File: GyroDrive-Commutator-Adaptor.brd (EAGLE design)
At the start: 127 x 76.2 mm, 30 parts, among them IC1 INA2141U, IC2 INA2141U, IC3 INA2141U

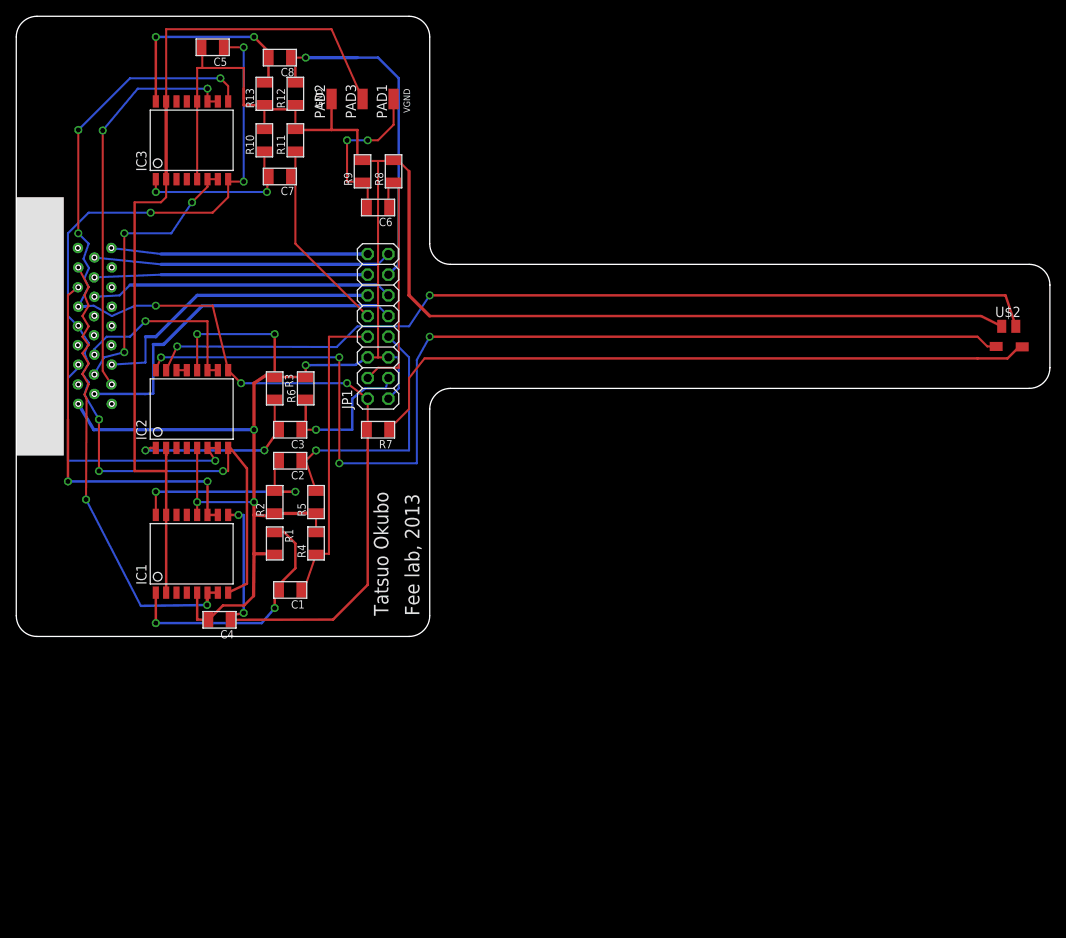
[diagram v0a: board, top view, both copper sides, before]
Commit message: Removed VGROUND and changed JMP1 pinout
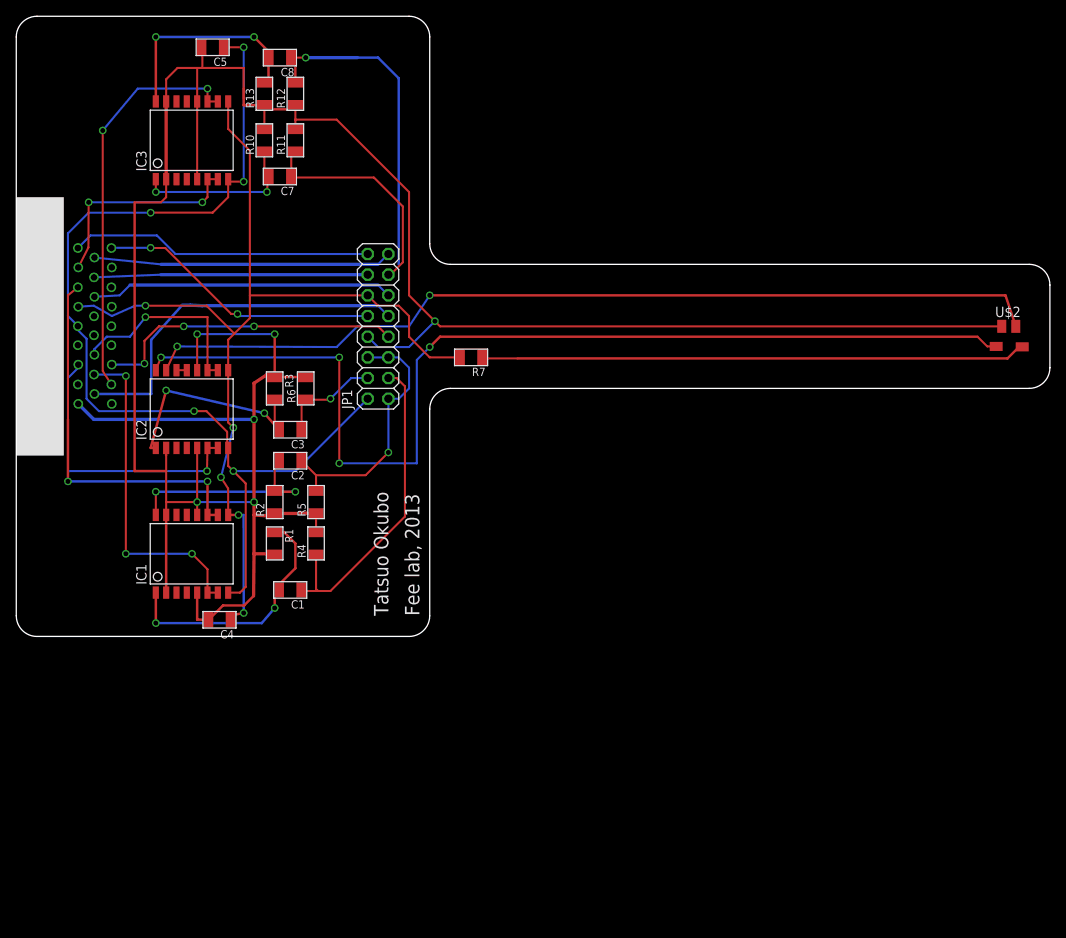
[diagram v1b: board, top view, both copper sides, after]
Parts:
- removed C6: 47nF, elm:R0805ELM
- removed PAD1, PAD2, PAD3: (no value), wirepad:SMD1,27-2,54
- removed R8: 22k, elm:R0805ELM
- removed R9: 1.5M, elm:R0805ELM
- moved R7 14.5 mm to (55.9, 34.3)
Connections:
- net STIM1OUT renamed SCL
- removed net FILTERED_VGROUND: C6.2, PAD1.1, R9.1
- removed net SIGNAL_GROUND: IC1.15, IC1.2, IC2.2, IC3.15, IC3.2, PAD3.1
- removed net STIM1IN: JP1.16, U$3._D
- removed net VGROUND: C6.1, JP1.4, R8.1
- new net DGND: JP1.16, U$3._C
- new net SDA: JP1.10, U$3._D
- net CHAN1: now also IC3.6, IC3.7; no longer IC1.6, IC1.7
- net CHAN4: now also IC1.6, IC1.7; no longer IC3.6, IC3.7
- net E1: now also C7.1, JP1.13, R11.1; no longer C1.1, JP1.8, R4.1
- net E2: now also JP1.1, JP1.5, JP1.6; no longer JP1.7
- net E3: now also JP1.4; no longer JP1.3
- net E4: now also C1.1, JP1.3, R4.1; no longer C7.1, JP1.10, R11.1
- net E5: no longer JP1.13
- net GROUND: now also IC1.15, IC1.2, IC2.2, IC3.15, IC3.2, JP1.8; no longer JP1.1, JP1.5, JP1.6, PAD2.1, R8.2, R9.2
- net ICOM: now also JP1.7; no longer JP1.12
- net V+: now also JP1.12; no longer JP1.2
- net V-: now also JP1.2
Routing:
- net SIGNAL_GROUND: track 110.1 -> 0.00 mm
- net GROUND: track 312.1 -> 352.5 mm
- net DGND: track 0.00 -> 37.2 mm
- net SDA: track 0.00 -> 35.0 mm, vias 0 -> 2
- net VGROUND: track 31.7 -> 0.00 mm
- net STIM1IN: track 31.5 -> 0.00 mm
- net CHAN1: track 56.6 -> 26.6 mm
- net V+: track 148.6 -> 121.2 mm, vias 8 -> 5
- net FILTERED_VGROUND: track 21.1 -> 0.00 mm, vias 2 -> 0
- net V+_HALL: track 84.6 -> 67.0 mm
- net E4: track 24.7 -> 39.5 mm
- net V-: track 116.0 -> 127.7 mm, vias 6 -> 5
- net E1: track 37.7 -> 27.8 mm
- net E3: track 19.6 -> 12.6 mm
- net CHAN4: track 34.9 -> 40.8 mm
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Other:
- board text removed: "GND"
- board text removed: "VGND"

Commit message: Made board into 4 layers. Put in resistors for voltage dividers
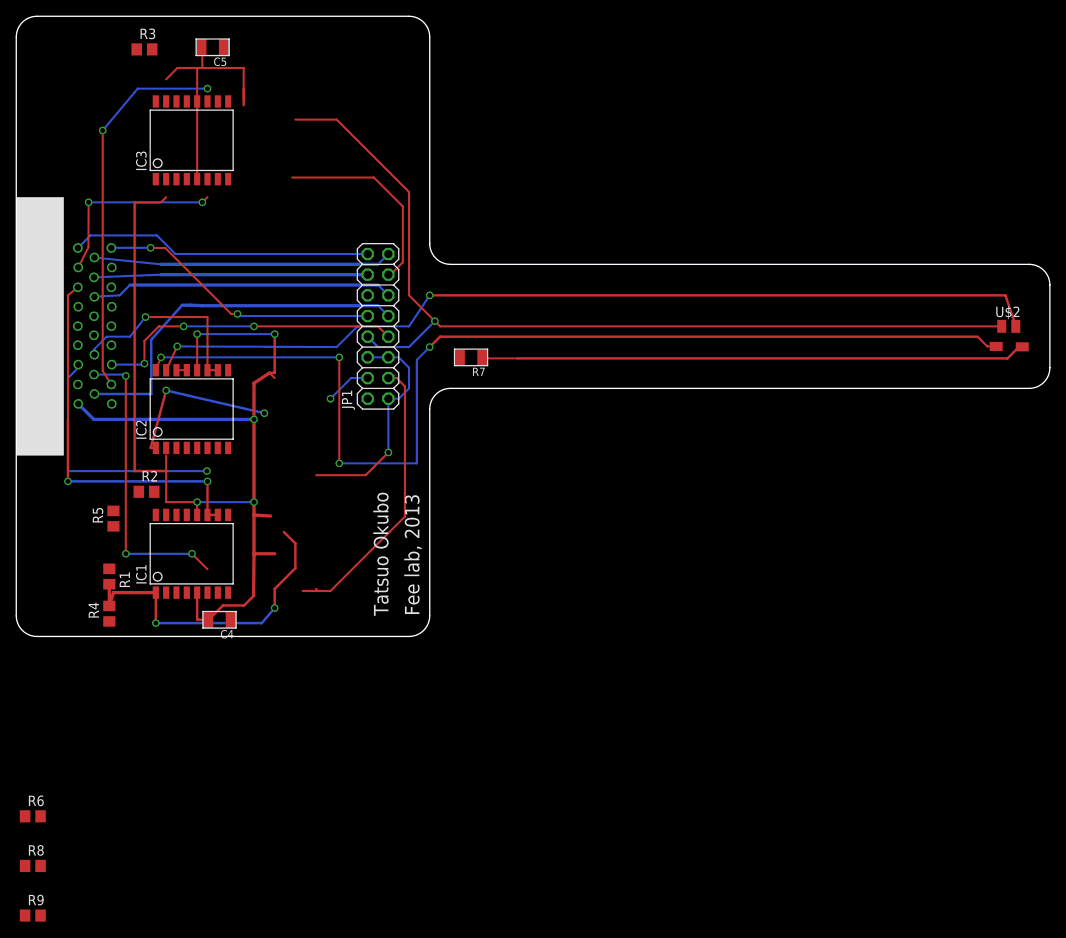
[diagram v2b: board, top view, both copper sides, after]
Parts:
- removed C1, C2, C3, C7, C8: 47nF, elm:R0805ELM
- removed R10, R13: 1.5M, elm:R0805ELM
- removed R11, R12: 22k, elm:R0805ELM
- added R8: 357k, resistor:R0805
- added R9: 3.6k, resistor:R0805
- R1: value 1.5M -> 3.6k; device elm:R0805ELM -> resistor:R0805
- R2, R3: value 1.5M -> 357k; device elm:R0805ELM -> resistor:R0805
- R4: value 22k -> 357k; device elm:R0805ELM -> resistor:R0805
- R5, R6: value 22k -> 3.6k; device elm:R0805ELM -> resistor:R0805
- moved R6 62.4 mm to (2.03, -22.1), turned to 0 degrees
- moved R3 44.6 mm to (15.7, 72.1), turned to 0 degrees
- moved R4 26.8 mm to (11.4, 2.79)
- moved R5 25.0 mm to (11.9, 14.5)
- moved R1 20.7 mm to (11.4, 7.37)
- moved R2 15.8 mm to (16.0, 17.8), turned to 0 degrees
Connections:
- removed net E5: C8.1, R12.2
- removed net GROUND: C4.2, C5.2, IC1.12, IC1.15, IC1.2, IC1.5, IC2.12, IC2.2, IC2.5, IC3.12, IC3.15, IC3.2, IC3.5, JP1.8, R1.2, R10.2, R11.2, R12.1, R13.1, R2.1, R3.1, R4.2, R5.1, R6.2, U$2.A, U$3.A
- removed net N$3: C2.2, IC1.16, R2.2
- removed net N$7: C8.2, IC3.16, R13.2
- removed net N$8: C7.2, IC3.1, R10.1
- new net AGND: C4.2, C5.2, IC1.12, IC1.15, IC1.2, IC1.5, IC2.12, IC3.12, IC3.15, IC3.2, IC3.5, JP1.8, R1.1, R5.1, R6.1, R9.1, U$2.A, U$3.A
- new net V-_INA1: IC1.16, R2.2, R5.2
- new net V-_INA2: IC3.1, R3.2, R6.2
- new net V-_INA3: IC3.16, R8.2, R9.2
- net CHAN1: now also IC1.6, IC1.7; no longer IC3.6, IC3.7
- net CHAN3: now also IC3.6, IC3.7; no longer IC2.6, IC2.7
- net CHAN4: now also IC3.10, IC3.11; no longer IC1.6, IC1.7
- net CHAN5: no longer IC3.10, IC3.11
- net E1: now also R4.1; no longer C7.1, R11.1
- net E2: now also R2.1; no longer C2.1, R5.2
- net E3: now also R3.1; no longer C3.1, R6.1
- net E4: now also R8.1; no longer C1.1, R4.1
- net V-_INA: now also R1.2, R4.2; no longer C1.2, R1.1
- net V-_INC: no longer C3.2, R3.2
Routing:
- net GROUND: track 352.5 -> 0.00 mm, vias 6 -> 0
- net AGND: track 0.00 -> 293.6 mm, vias 0 -> 6
- net V-: track 127.7 -> 0.00 mm, vias 5 -> 0
- net V+: track 121.2 -> 0.00 mm, vias 5 -> 0
- net E5: track 40.2 -> 0.00 mm, vias 1 -> 0
- net N$7: track 26.8 -> 0.00 mm, vias 2 -> 0
- net N$3: track 26.5 -> 0.00 mm, vias 2 -> 0
- net N$8: track 21.6 -> 0.00 mm, vias 2 -> 0
- net V-_INA: track 31.8 -> 39.8 mm
- net V-_INC: track 27.4 -> 20.3 mm
- net E3: track 12.6 -> 5.80 mm
- net E2: track 32.4 -> 27.9 mm
- net E4: track 39.5 -> 35.2 mm
- net CHAN4: track 40.8 -> 36.7 mm
- net CHAN3: track 34.8 -> 30.7 mm
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- added copper zone on layer 15, net AGND

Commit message: Finished routing
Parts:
- removed IC1, IC2, IC3: INA2141U, burr-brown:SO16-1
- removed U$3: MMD1P22G-26-M101, elm:MMD1P22G-26-M101
- added C1, C2, C3, C6: (no value), resistor:C0402
- added U$1: NORCOMP-DB25-SMD-MALE, michael-stetner:190-025-163R001
- added U1, U2, U3: INA2141U, burr-brown:SO16-1
- added U4: PCA9517, PCA9517:SO-08
- added U5: 5V, michael-stetner:SC70
- added U6: 2.5V, michael-stetner:SC70
- moved R9 92.1 mm to (15.1, 56.9), turned to 180 degrees
- moved R8 86.8 mm to (19.1, 56.9), turned to 180 degrees
- moved C5 57.5 mm to (8.26, 17.2), turned to 270 degrees
- moved R6 50.5 mm to (15.1, 26.7), turned to 180 degrees
- moved R3 45.5 mm to (19.1, 26.7), turned to 180 degrees
- moved R4 18.9 mm to (19.1, 20.1), turned to 180 degrees
- moved C4 17.7 mm to (8.24, 7.75), turned to 90 degrees
- moved JP1 17.3 mm to (27.2, 38.1)
- moved R2 13.4 mm to (19.1, 4.80), turned to 180 degrees
- moved R1 13.2 mm to (15.1, 20.1), turned to 0 degrees
- moved R5 10.2 mm to (15.1, 4.80), turned to 180 degrees
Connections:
- removed net CHAN5: U$3.F
- removed net GAIN_HALL: IC2.13, IC2.14
- removed net MOTOR_GROUND: U$3._B
- removed net SCL: JP1.15, U$3._A
- removed net SDA: JP1.10, U$3._D
- removed net STIM2IN: JP1.11, U$3.U
- removed net STIM2OUT: JP1.14, U$3.X
- removed net V-_INA: IC1.1, R1.2, R4.2
- removed net V-_INA1: IC1.16, R2.2, R5.2
- removed net V-_INA2: IC3.1, R3.2, R6.2
- removed net V-_INA3: IC3.16, R8.2, R9.2
- removed net V-_INC: IC2.1
- new net +2.5V: C6.1, U4.1, U6.5
- new net +5V: C1.1, U4.5, U4.8, U5.5
- new net IN1: R2.2, R5.1, U1.15
- new net IN2: R1.2, R4.2, U1.2
- new net IN3: R3.2, R6.1, U2.15
- new net IN4: R8.2, R9.1, U3.2
- new net MOTORGND: U$1.P$18
- new net N$1: U2.6, U2.7
- new net N$3: U3.13, U3.14
- new net SCL_BIRD: JP1.16, U4.2
- new net SCL_RIG: U$1.P$22, U4.7
- new net SDA_BIRD: JP1.15, U4.3
- new net SDA_RIG: U$1.P$21, U4.6
- new net STIMIN: JP1.5, U$1.P$23
- new net STIMOUT: JP1.3, U$1.P$24
- net AGND: now also JP1.10, JP1.11, R5.2, R6.2, R9.2, U$1.P$10, U1.1, U1.12, U1.16, U1.5, U2.1, U2.12, U2.16, U2.2, U3.1, U3.12, U3.5; no longer IC1.12, IC1.15, IC1.2, IC1.5, IC2.12, IC3.12, IC3.15, IC3.2, IC3.5, JP1.8, R5.1, R6.1, R9.1, U$3.A
- net CHAN1: now also U$1.P$13, U1.10, U1.11; no longer IC1.6, IC1.7, U$3.Z
- net CHAN2: now also U$1.P$12, U1.6, U1.7; no longer IC1.10, IC1.11, U$3.W
- net CHAN3: now also U$1.P$11, U2.10, U2.11; no longer IC3.6, IC3.7, U$3.H
- net CHAN4: now also U$1.P$16, U3.6, U3.7; no longer IC3.10, IC3.11, U$3.E
- net DGND: now also C1.2, C2.2, C3.2, C6.2, JP1.13, JP1.14, U$1.P$15, U4.4, U5.2, U6.2; no longer JP1.16, U$3._C
- net E1: now also JP1.1, R2.1; no longer JP1.13, R4.1
- net E2: now also JP1.2, R4.1; no longer JP1.1, JP1.5, JP1.6, R2.1
- net E4: now also JP1.12; no longer JP1.3
- net HALL: now also U$1.P$4, U3.10, U3.11; no longer IC2.10, IC2.11, U$3.J
- net HALL0: now also U3.16; no longer IC2.16
- net HALL1: now also U3.15; no longer IC2.15
- net ICOM: now also JP1.6, U$1.P$5; no longer JP1.7, U$3.K
- net IX: now also JP1.8, U$1.P$17; no longer JP1.9, U$3.B
- net V+: now also C2.1, C3.1, JP1.9, U$1.P$1, U1.9, U2.9, U3.9, U5.4, U6.4; no longer IC1.9, IC2.9, IC3.9, JP1.12, U$3.T
- net V-: now also JP1.7, U$1.P$2, U1.8, U2.8, U3.8; no longer IC1.8, IC2.8, IC3.8, JP1.2, U$3.P
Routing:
- net V+: track 0.00 -> 185.1 mm, vias 0 -> 5
- net AGND: track 293.6 -> 116.9 mm, vias 6 -> 14
- net V-: track 0.00 -> 73.9 mm, vias 0 -> 5
- net SCL_RIG: track 0.00 -> 53.5 mm, vias 0 -> 2
- net SDA_RIG: track 0.00 -> 50.1 mm, vias 0 -> 2
- net CHAN5: track 46.8 -> 0.00 mm, vias 2 -> 0
- net V-_INA: track 39.8 -> 0.00 mm, vias 2 -> 0
- net STIM2IN: track 37.2 -> 0.00 mm
- net SCL: track 36.7 -> 0.00 mm
- net SDA: track 35.0 -> 0.00 mm, vias 2 -> 0
- net STIM2OUT: track 33.6 -> 0.00 mm
- net STIMOUT: track 0.00 -> 33.0 mm, vias 0 -> 1
- net SDA_BIRD: track 0.00 -> 29.1 mm, vias 0 -> 1
- net STIMIN: track 0.00 -> 28.7 mm, vias 0 -> 1
- net CHAN2: track 47.0 -> 19.2 mm, vias 2 -> 0
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- added copper zone on layer 15, net DGND

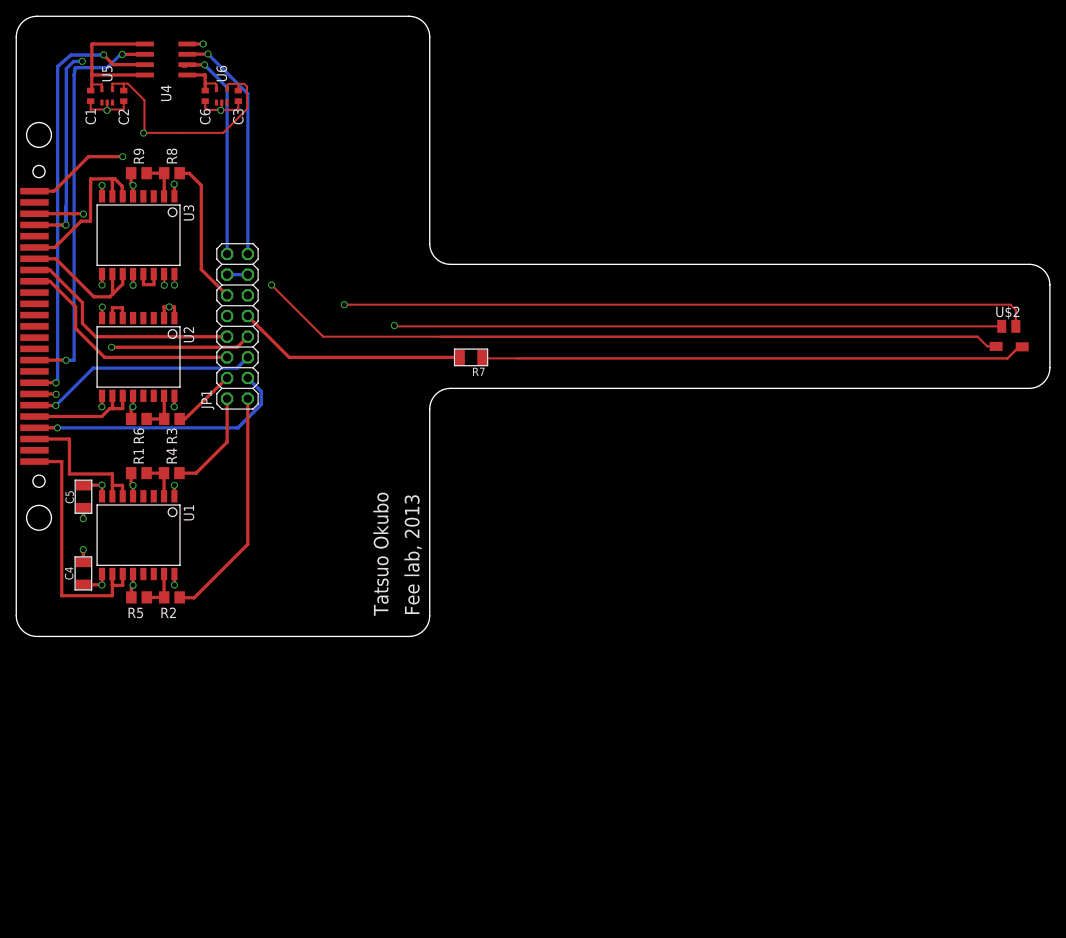
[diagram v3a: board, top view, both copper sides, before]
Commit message: added parts list
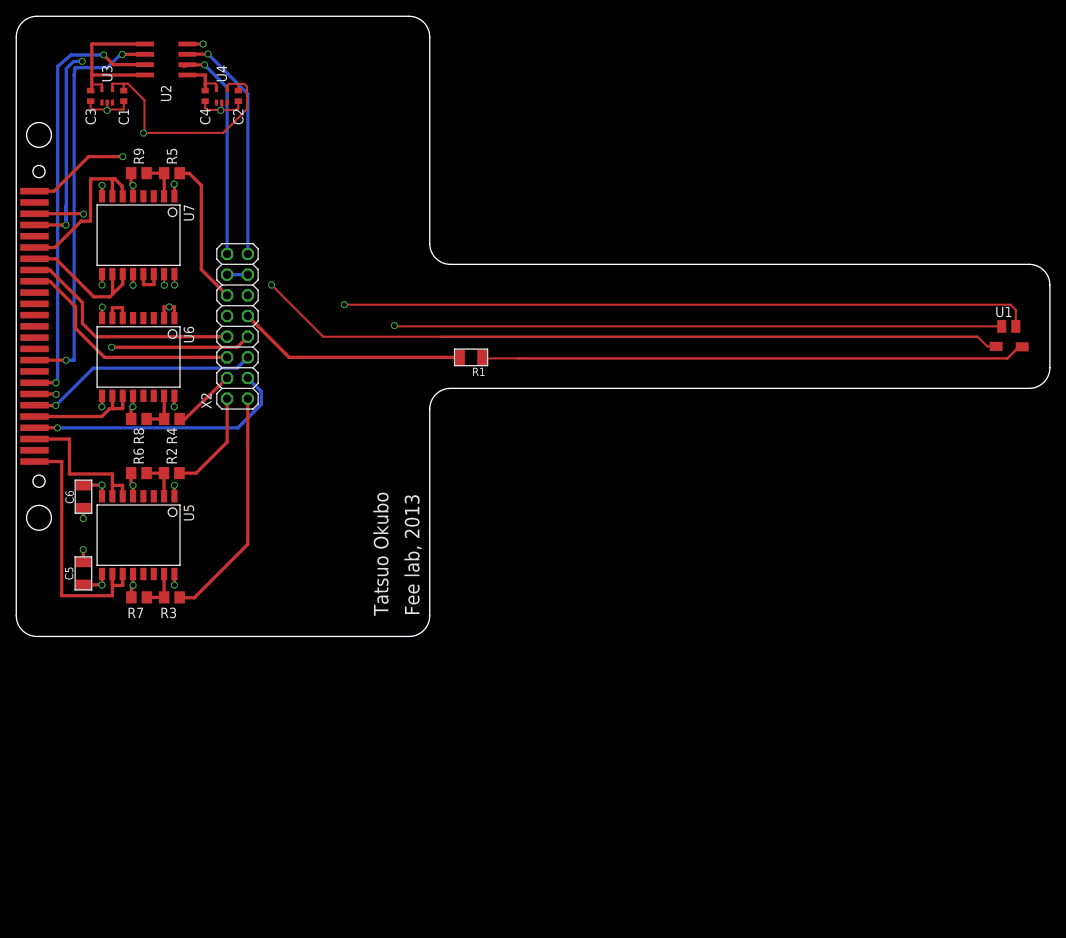
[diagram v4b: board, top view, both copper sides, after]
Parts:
- removed U$2: HALL, elm:HALL_ON_SIDE
- added U7: INA2141U, burr-brown:SO16-1
- C4: value 100nF -> (none); device elm:R0805ELM -> resistor:C0402
- C6: value (none) -> 100nF; device resistor:C0402 -> elm:R0805ELM
- R1: value 3.6k -> 10k; device resistor:R0805 -> elm:R0805ELM
- R5: value 3.6k -> 357k
- R7: value 10k -> 3.6k; device elm:R0805ELM -> resistor:R0805
- R8: value 357k -> 3.6k
- U1: value INA2141U -> HALL; device burr-brown:SO16-1 -> elm:HALL_ON_SIDE
- U2: value INA2141U -> PCA9517; device burr-brown:SO16-1 -> PCA9517:SO-08
- U3: value INA2141U -> 5V; device burr-brown:SO16-1 -> michael-stetner:SC70
- U4: value PCA9517 -> 2.5V; device PCA9517:SO-08 -> michael-stetner:SC70
- U5: value 5V -> INA2141U; device michael-stetner:SC70 -> burr-brown:SO16-1
- U6: value 2.5V -> INA2141U; device michael-stetner:SC70 -> burr-brown:SO16-1
- moved U1 110.0 mm to (121.9, 38.1), turned to 0 degrees
- moved C4 60.6 mm to (23.2, 66.4), turned to 270 degrees
- moved U5 54.1 mm to (15.0, 12.4), turned to 180 degrees
- moved R5 52.3 mm to (19.1, 56.9)
- moved C6 51.5 mm to (8.26, 17.2)
- moved R7 50.3 mm to (15.1, 4.80)
- moved R1 43.2 mm to (55.9, 34.3), turned to 180 degrees
- moved U2 36.7 mm to (18.4, 70.9), turned to 90 degrees
- moved U6 33.7 mm to (15.0, 34.3), turned to 180 degrees
- moved R8 30.5 mm to (15.1, 26.7)
- moved R3 21.9 mm to (19.1, 4.80)
- moved C3 18.1 mm to (9.14, 66.4)
- moved U3 17.5 mm to (11.2, 66.4), turned to 0 degrees
- moved R2 15.3 mm to (19.1, 20.1)
- moved C2 14.1 mm to (27.3, 66.4)
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- renumbered JP1 to X2, U$1 to X1
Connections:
- net +2.5V: now also C4.1, U2.1, U4.5; no longer C6.1, U4.1, U6.5
- net +5V: now also C3.1, U2.5, U2.8, U3.5; no longer C1.1, U4.5, U4.8, U5.5
- net AGND: now also C6.2, R6.1, R7.2, R8.2, U1.A, U5.1, U5.12, U5.16, U5.5, U6.1, U6.12, U6.16, U6.2, U7.1, U7.12, U7.5; no longer C4.2, R1.1, R5.2, R6.2, U$2.A, U1.1, U1.12, U1.16, U1.5, U2.1, U2.12, U2.16, U2.2, U3.1, U3.12, U3.5
- net CHAN1: now also U5.10, U5.11; no longer U1.10, U1.11
- net CHAN2: now also U5.6, U5.7; no longer U1.6, U1.7
- net CHAN3: now also U6.10, U6.11; no longer U2.10, U2.11
- net CHAN4: now also U7.6, U7.7; no longer U3.6, U3.7
- net DGND: now also C4.2, U2.4, U3.2, U4.2; no longer C6.2, U4.4, U5.2, U6.2
- net E1: now also R3.1; no longer R2.1
- net E2: now also R2.1; no longer R4.1
- net E3: now also R4.1; no longer R3.1
- net E4: now also R5.1; no longer R8.1
- net HALL: now also U7.10, U7.11; no longer U3.10, U3.11
- net HALL0: now also U1.D, U7.16; no longer U$2.D, U3.16
- net HALL1: now also U1.B, U7.15; no longer U$2.B, U3.15
- net IN1: now also R3.2, R7.1, U5.15; no longer R2.2, R5.1, U1.15
- net IN2: now also R2.2, R6.2, U5.2; no longer R1.2, R4.2, U1.2
- net IN3: now also R4.2, R8.1, U6.15; no longer R3.2, R6.1, U2.15
- net IN4: now also R5.2, U7.2; no longer R8.2, U3.2
- net N$1: now also U6.6, U6.7; no longer U2.6, U2.7
- net N$3: now also U7.13, U7.14; no longer U3.13, U3.14
- net SCL_BIRD: now also U2.2; no longer U4.2
- net SCL_RIG: now also U2.7; no longer U4.7
- net SDA_BIRD: now also U2.3; no longer U4.3
- net SDA_RIG: now also U2.6; no longer U4.6
- net V+: now also C1.1, C5.1, R1.2, U3.4, U4.4, U5.9, U6.9, U7.9; no longer C3.1, C4.1, R7.2, U1.9, U2.9, U3.9, U5.4, U6.4
- net V+_HALL: now also R1.1, U1.C; no longer R7.1, U$2.C
- net V-: now also C6.1, U5.8, U6.8, U7.8; no longer C5.1, U1.8, U2.8, U3.8
